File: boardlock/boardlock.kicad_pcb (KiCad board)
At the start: 2 copper layers, 101 x 76.2 mm, 131 parts, among them J1 Conn_01x02, J2 Conn_01x02, J3 Conn_01x02, J4 Conn_01x02, J5 5033981892, J6 USB_C_Receptacle_USB2.0, Q1 BSS84PWH6327XTSA1, Q2 MMBT4401, Q3 BSS84PWH6327XTSA1, Q4 DTC124X, Q5 DTC124X, Q6 DTC124X, Q7 DTC124X, SW1 SW_Push, SW2 SW_Push, SW3 TL3300DF160Q, SW4 SW_Push, SW5 TL3300DF160Q, U1 ESP32-S3-WROOM-1, U2 LSM6DSO32, U3 SAM-M8Q, U4 BQ24075RGT, U5 BQ27441DRZR-G1A, U6 TPS630701RNMR, U7 MCP1661, U8 MAX98357AETE+T, U9 TPD2E2U06

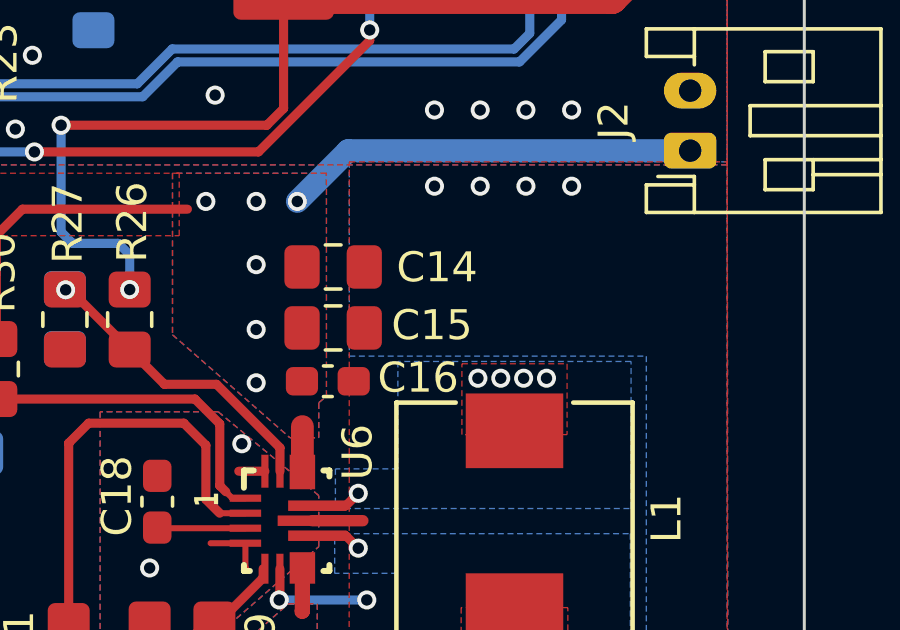
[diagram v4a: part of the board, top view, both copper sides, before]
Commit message: added some GND vias
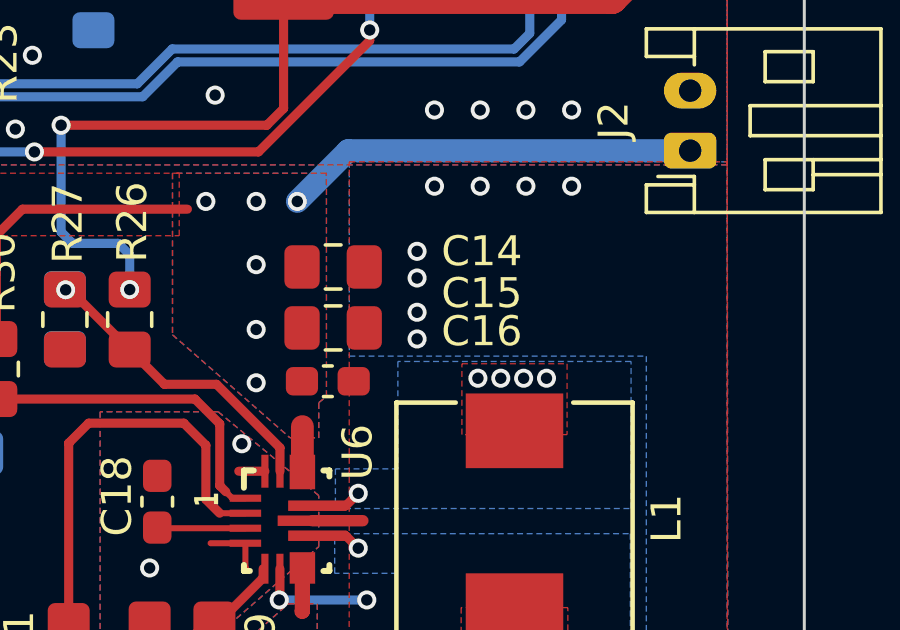
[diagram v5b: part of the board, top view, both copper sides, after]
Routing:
- net GND: vias 304 -> 308
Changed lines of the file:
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@@
     (clearance 0.254)
     (attr smd)
-    (fp_text reference "C14" (at 3.4631 0.0136) (layer "F.SilkS")
+    (fp_text reference "C14" (at 4.9561 -0.5214) (layer "F.SilkS")
         (effects (font (size 1 1) (thickness 0.15)))
     )
@@
     (clearance 0.254)
     (attr smd)
-    (fp_text reference "C16" (at 3.0109 -0.1164 180) (layer "F.SilkS")
+    (fp_text reference "C16" (at 5.1339 -1.6644 180) (layer "F.SilkS")
         (effects (font (size 1 1) (thickness 0.15)))
     )
@@
     (clearance 0.254)
     (attr smd)
-    (fp_text reference "C15" (at 3.2931 -0.0884) (layer "F.SilkS")
+    (fp_text reference "C15" (at 4.9561 -1.1564) (layer "F.SilkS")
         (effects (font (size 1 1) (thickness 0.15)))
     )
@@
   (via (at 137.53 115.1) (size 0.635) (drill 0.381) (layers "F.Cu" "B.Cu") (free) (net 103))
   (via (at 197.358 78.994) (size 0.635) (drill 0.381) (layers "F.Cu" "B.Cu") (free) (net 103))
+  (via (at 195.254 83.705) (size 0.635) (drill 0.381) (layers "F.Cu" "B.Cu") (free) (net 103))
   (via (at 169.418 70.104) (size 0.635) (drill 0.381) (layers "F.Cu" "B.Cu") (free) (net 103))
   (via (at 169.9768 105.4608) (size 0.635) (drill 0.381) (layers "F.Cu" "B.Cu") (free) (net 103))
@@
   (via (at 128.06 99.3) (size 0.635) (drill 0.381) (layers "F.Cu" "B.Cu") (free) (net 103))
   (via (at 125.18 120.68) (size 0.635) (drill 0.381) (layers "F.Cu" "B.Cu") (free) (net 103))
+  (via (at 195.254 84.594) (size 0.635) (drill 0.381) (layers "F.Cu" "B.Cu") (free) (net 103))
   (via (at 119.64 75.816) (size 0.635) (drill 0.381) (layers "F.Cu" "B.Cu") (free) (net 103))
   (via (at 162.72 115.75) (size 0.635) (drill 0.381) (layers "F.Cu" "B.Cu") (free) (net 103))
@@
   (via (at 113.57 120.56) (size 0.635) (drill 0.381) (layers "F.Cu" "B.Cu") (free) (net 103))
   (via (at 188.523 78.498) (size 0.635) (drill 0.381) (layers "F.Cu" "B.Cu") (free) (net 103))
+  (via (at 195.254 86.626) (size 0.635) (drill 0.381) (layers "F.Cu" "B.Cu") (free) (net 103))
   (via (at 122.48 111.52) (size 0.635) (drill 0.381) (layers "F.Cu" "B.Cu") (free) (net 103))
   (via (at 152.56 107.58) (size 0.635) (drill 0.381) (layers "F.Cu" "B.Cu") (free) (net 103))
@@
   (via (at 135.85 124.35) (size 0.635) (drill 0.381) (layers "F.Cu" "B.Cu") (free) (net 103))
   (via (at 134.83 104.84) (size 0.635) (drill 0.381) (layers "F.Cu" "B.Cu") (free) (net 103))
+  (via (at 195.254 85.737) (size 0.635) (drill 0.381) (layers "F.Cu" "B.Cu") (free) (net 103))
   (via (at 144.21 100.41) (size 0.635) (drill 0.381) (layers "F.Cu" "B.Cu") (free) (net 103))
   (via (at 127.84 120.19) (size 0.635) (drill 0.381) (layers "F.Cu" "B.Cu") (free) (net 103))

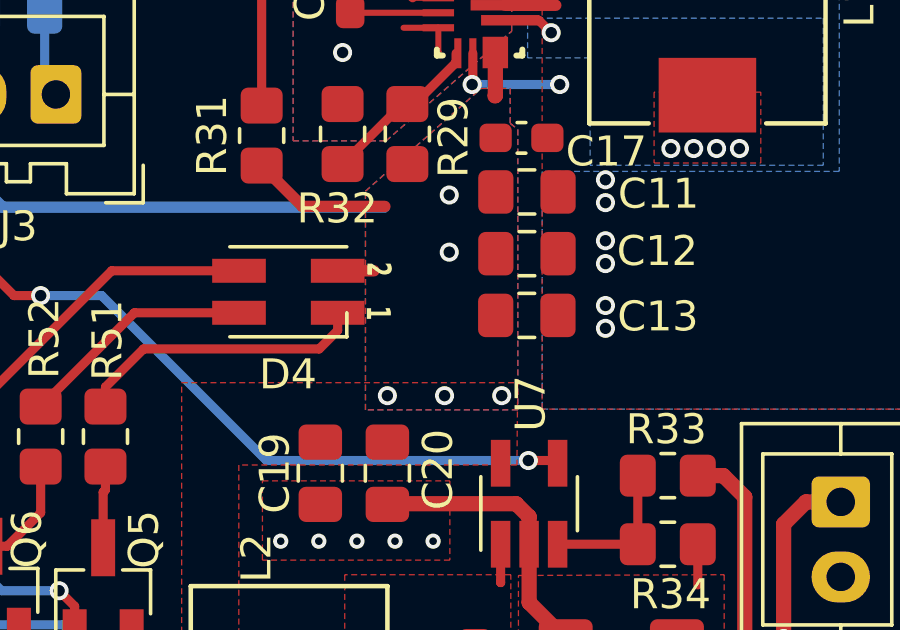
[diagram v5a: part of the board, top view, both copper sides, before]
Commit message: another via got deleted
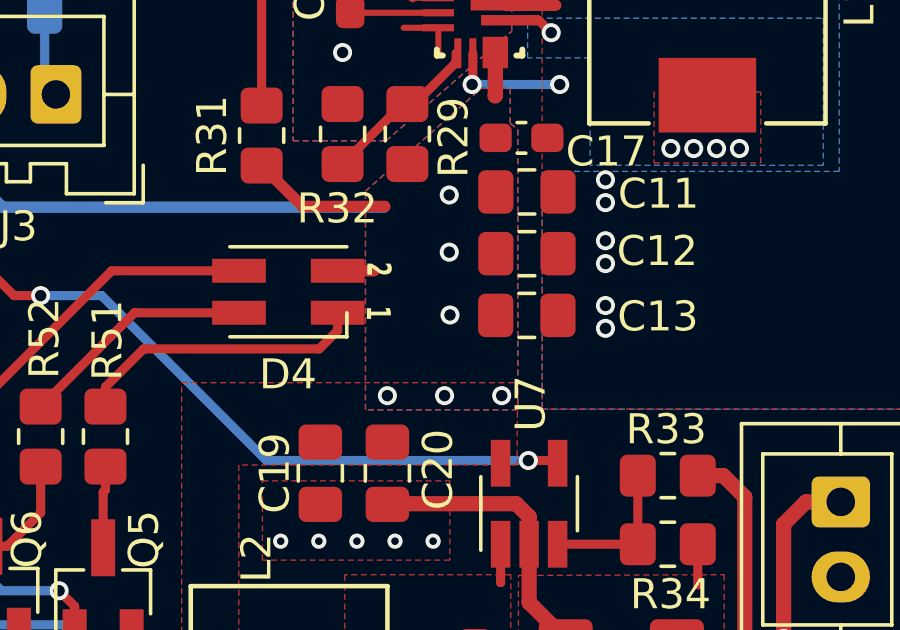
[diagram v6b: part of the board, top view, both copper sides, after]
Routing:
- net +3V3: vias 20 -> 21
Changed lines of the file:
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@@
   (via (at 162.687 82.042) (size 0.635) (drill 0.381) (layers "F.Cu" "B.Cu") (net 1))
   (via (at 189.738 105.6971) (size 0.635) (drill 0.381) (layers "F.Cu" "B.Cu") (free) (net 1))
+  (via (at 189.92 103.009) (size 0.635) (drill 0.381) (layers "F.Cu" "B.Cu") (free) (net 1))
   (via (at 116.29 128.06) (size 0.635) (drill 0.381) (layers "F.Cu" "B.Cu") (net 1))
   (via (at 191.643 105.6971) (size 0.635) (drill 0.381) (layers "F.Cu" "B.Cu") (free) (net 1))

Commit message: small edits
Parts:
- R14: value R_US -> 0
- R8, R9: value R_US -> 22
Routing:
- net GND: vias 308 -> 318
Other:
- board text added: "ECE477 Group 13 10-13-2023, Version 1.0 Zecong Liang Nicholas Williams Jamie Lam David Reed"
- board text removed: "TEAM 13 10-12-2023, Version 1.0 Zecong Liang Nicholas Williams Jamie Lam David Reed"
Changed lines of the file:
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@@
         (effects (font (size 1 1) (thickness 0.15)))
     )
-    (fp_text value "R_US" (at 0 1.65 90) (layer "F.Fab")
+    (fp_text value "22" (at 0 1.65 90) (layer "F.Fab")
         (effects (font (size 1 1) (thickness 0.15)))
     )
@@
         (effects (font (size 1 1) (thickness 0.15)))
     )
-    (fp_text value "R_US" (at 0 1.65 90) (layer "F.Fab")
+    (fp_text value "22" (at 0 1.65 90) (layer "F.Fab")
         (effects (font (size 1 1) (thickness 0.15)))
     )
@@
         (effects (font (size 1 1) (thickness 0.15)) (justify mirror))
     )
-    (fp_text value "R_US" (at 0 -1.65) (layer "B.Fab")
+    (fp_text value "0" (at 0 -1.65) (layer "B.Fab")
         (effects (font (size 1 1) (thickness 0.15)) (justify mirror))
     )
@@
   (gr_rect (start 106.92 65.9) (end 133.55 85.48)
     (stroke (width 0.15) (type default)) (fill none) (layer "User.2"))
-  (gr_text "TEAM 13\n10-12-2023, Version 1.0\nZecong Liang\nNicholas Williams\nJamie Lam\nDavid Reed" (at 160.8 125.9) (layer "B.SilkS")
+  (gr_text "ECE477 Group 13\n10-13-2023, Version 1.0\nZecong Liang\nNicholas Williams\nJamie Lam\nDavid Reed" (at 160.8 125.9) (layer "B.SilkS")
     (effects (font (size 2 2) (thickness 0.3) bold) (justify left bottom mirror))
   )
@@
   (via (at 149.83 105.94) (size 0.635) (drill 0.381) (layers "F.Cu" "B.Cu") (free) (net 103))
   (via (at 152.26 120.54) (size 0.635) (drill 0.381) (layers "F.Cu" "B.Cu") (free) (net 103))
+  (via (at 116.63 136.81) (size 0.635) (drill 0.381) (layers "F.Cu" "B.Cu") (free) (net 103))
   (via (at 184.15 68.961) (size 0.635) (drill 0.381) (layers "F.Cu" "B.Cu") (net 103))
   (via (at 132.84 93.77) (size 0.635) (drill 0.381) (layers "F.Cu" "B.Cu") (free) (net 103))
@@
   (via (at 153.86 101.83) (size 0.635) (drill 0.381) (layers "F.Cu" "B.Cu") (free) (net 103))
   (via (at 155.85 131.03) (size 0.635) (drill 0.381) (layers "F.Cu" "B.Cu") (free) (net 103))
-  (via (at 117.74 130.4) (size 0.635) (drill 0.381) (layers "F.Cu" "B.Cu") (free) (net 103))
+  (via (at 117.9 129.74) (size 0.635) (drill 0.381) (layers "F.Cu" "B.Cu") (free) (net 103))
   (via (at 151.11 99.92) (size 0.635) (drill 0.381) (layers "F.Cu" "B.Cu") (free) (net 103))
   (via (at 139.34 118.82) (size 0.635) (drill 0.381) (layers "F.Cu" "B.Cu") (free) (net 103))
@@
   (via (at 157.93 94.3) (size 0.635) (drill 0.381) (layers "F.Cu" "B.Cu") (free) (net 103))
   (via (at 195.834 78.994) (size 0.635) (drill 0.381) (layers "F.Cu" "B.Cu") (free) (net 103))
+  (via (at 188.26 129.96) (size 0.635) (drill 0.381) (layers "F.Cu" "B.Cu") (free) (net 103))
   (via (at 178.8522 75.2081) (size 0.635) (drill 0.381) (layers "F.Cu" "B.Cu") (net 103))
   (via (at 162.91 109.73) (size 0.635) (drill 0.381) (layers "F.Cu" "B.Cu") (free) (net 103))
@@
   (via (at 173.99 70.866) (size 0.635) (drill 0.381) (layers "F.Cu" "B.Cu") (net 103))
   (via (at 176.276 79.629) (size 0.635) (drill 0.381) (layers "F.Cu" "B.Cu") (free) (net 103))
+  (via (at 175.07 127.96) (size 0.635) (drill 0.381) (layers "F.Cu" "B.Cu") (free) (net 103))
   (via (at 147.04 125.37) (size 0.635) (drill 0.381) (layers "F.Cu" "B.Cu") (free) (net 103))
   (via (at 127.35 111.56) (size 0.635) (drill 0.381) (layers "F.Cu" "B.Cu") (free) (net 103))
@@
   (via (at 140.54 117.76) (size 0.635) (drill 0.381) (layers "F.Cu" "B.Cu") (free) (net 103))
   (via (at 144.16 97.45) (size 0.635) (drill 0.381) (layers "F.Cu" "B.Cu") (free) (net 103))
+  (via (at 188.32 133.27) (size 0.635) (drill 0.381) (layers "F.Cu" "B.Cu") (free) (net 103))
   (via (at 162.58 112.62) (size 0.635) (drill 0.381) (layers "F.Cu" "B.Cu") (free) (net 103))
   (via (at 139.21 116.52) (size 0.635) (drill 0.381) (layers "F.Cu" "B.Cu") (free) (net 103))
+  (via (at 171.86 137.48) (size 0.635) (drill 0.381) (layers "F.Cu" "B.Cu") (free) (net 103))
   (via (at 129.74 115.68) (size 0.635) (drill 0.381) (layers "F.Cu" "B.Cu") (free) (net 103))
   (via (at 153.37 96.38) (size 0.635) (drill 0.381) (layers "F.Cu" "B.Cu") (free) (net 103))
@@
   (via (at 135.36 121.21) (size 0.635) (drill 0.381) (layers "F.Cu" "B.Cu") (free) (net 103))
   (via (at 195.1024 100.5332) (size 0.635) (drill 0.381) (layers "F.Cu" "B.Cu") (free) (net 103))
+  (via (at 188.49 136.98) (size 0.635) (drill 0.381) (layers "F.Cu" "B.Cu") (free) (net 103))
   (via (at 134.47 135.85) (size 0.635) (drill 0.381) (layers "F.Cu" "B.Cu") (free) (net 103))
   (via (at 130.53 76.04) (size 0.635) (drill 0.381) (layers "F.Cu" "B.Cu") (free) (net 103))
   (via (at 122.39 121.16) (size 0.635) (drill 0.381) (layers "F.Cu" "B.Cu") (free) (net 103))
+  (via (at 177.88 127.87) (size 0.635) (drill 0.381) (layers "F.Cu" "B.Cu") (free) (net 103))
+  (via (at 116.68 134.25) (size 0.635) (drill 0.381) (layers "F.Cu" "B.Cu") (free) (net 103))
   (via (at 152.48 134.04) (size 0.635) (drill 0.381) (layers "F.Cu" "B.Cu") (free) (net 103))
   (via (at 142.58 89.76) (size 0.635) (drill 0.381) (layers "F.Cu" "B.Cu") (free) (net 103))
@@
   (via (at 136.42 129.7) (size 0.635) (drill 0.381) (layers "F.Cu" "B.Cu") (free) (net 103))
   (via (at 159.56 136.12) (size 0.635) (drill 0.381) (layers "F.Cu" "B.Cu") (free) (net 103))
+  (via (at 179.91 137.34) (size 0.635) (drill 0.381) (layers "F.Cu" "B.Cu") (free) (net 103))
   (via (at 135.85 124.35) (size 0.635) (drill 0.381) (layers "F.Cu" "B.Cu") (free) (net 103))
   (via (at 134.83 104.84) (size 0.635) (drill 0.381) (layers "F.Cu" "B.Cu") (free) (net 103))
@@
   (via (at 145.18 113.55) (size 0.635) (drill 0.381) (layers "F.Cu" "B.Cu") (free) (net 103))
   (via (at 137.31 112.76) (size 0.635) (drill 0.381) (layers "F.Cu" "B.Cu") (free) (net 103))
+  (via (at 176.02 137.31) (size 0.635) (drill 0.381) (layers "F.Cu" "B.Cu") (free) (net 103))
   (via (at 159.43 131.08) (size 0.635) (drill 0.381) (layers "F.Cu" "B.Cu") (free) (net 103))
   (via (at 181.864 79.629) (size 0.635) (drill 0.381) (layers "F.Cu" "B.Cu") (free) (net 103))
